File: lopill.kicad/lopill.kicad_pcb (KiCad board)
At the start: 2 copper layers, 23 x 59.5 mm, 34 parts, among them J1 Pins Left, J2 SWD, J3 USB_B_Micro, J4 Pins Right, SW1 Reset, U1 XC6206PxxxMR, U2 STM32L052C8Tx, Y1 8MHz, Y2 32.768KHz

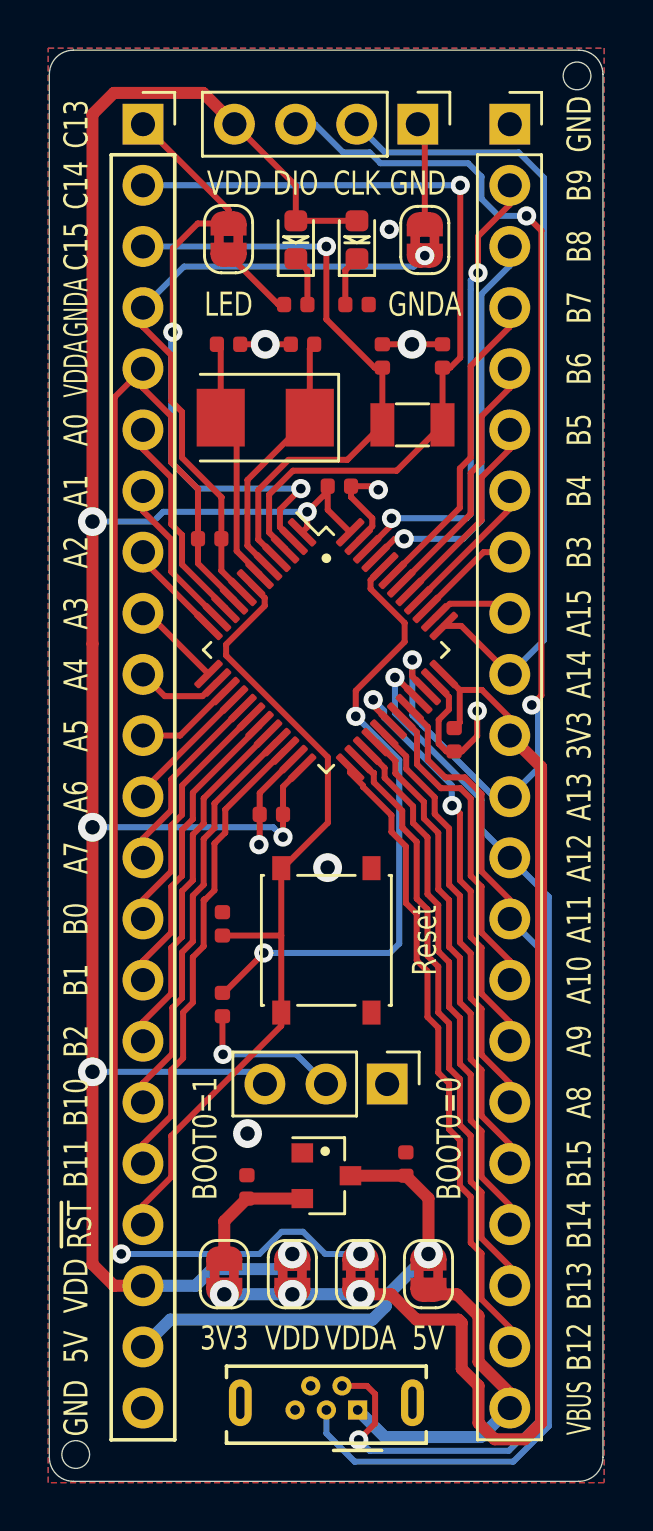
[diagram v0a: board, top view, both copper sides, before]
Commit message: Upgrade to KiCAD v6
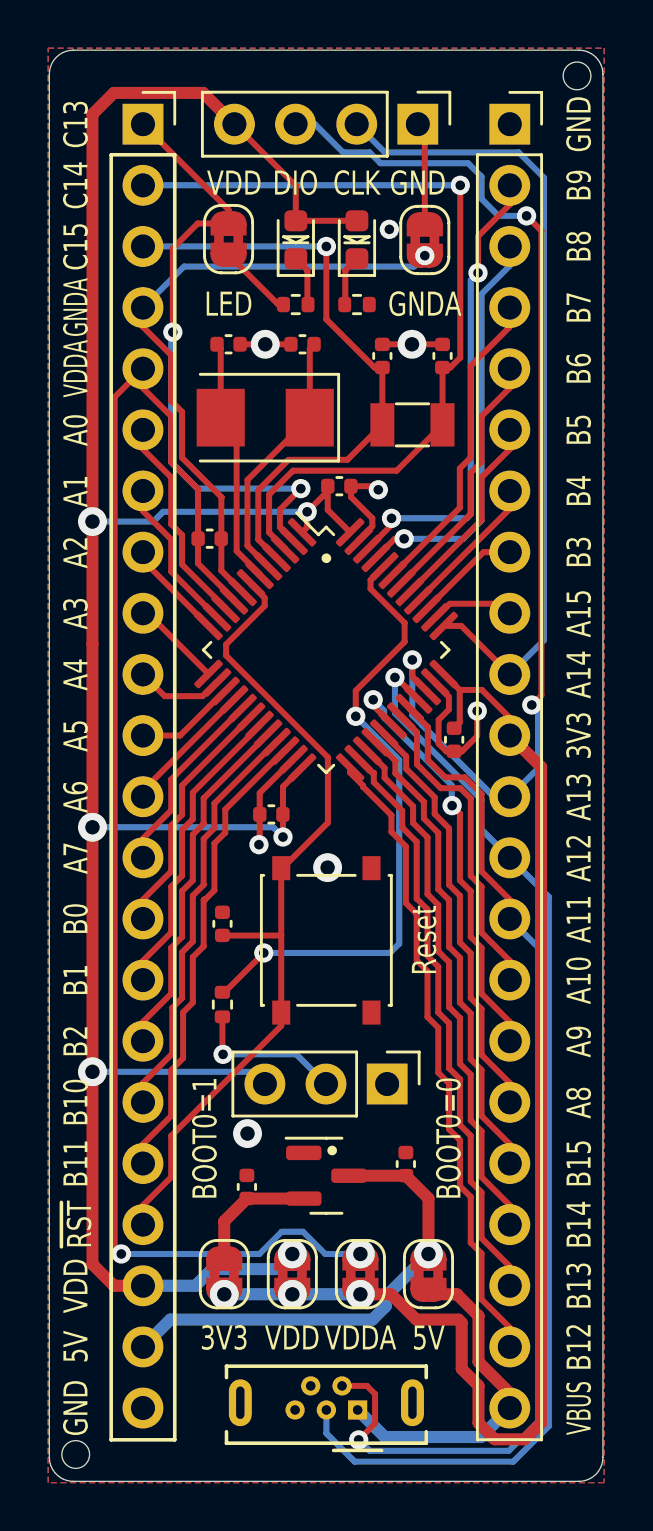
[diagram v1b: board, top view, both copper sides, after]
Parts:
- J3: footprint lopill:USB_Micro-B_HRO_U-D-M5DD-W-1_Vertical -> spbnick:USB_Micro-B_HRO_U-D-M5DD-W-1_Vertical
- REF** (x2): footprint lopill:Tooling_Hole -> spbnick:Tooling_Hole
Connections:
- J3 pad 4: Net-(J3-Pad4) -> unconnected-(J3-Pad4)
- J3 pad 6: GND -> unconnected-(J3-Pad6)
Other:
- net class Default removed
- net class Power removed

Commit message: Move footprints to the shared library
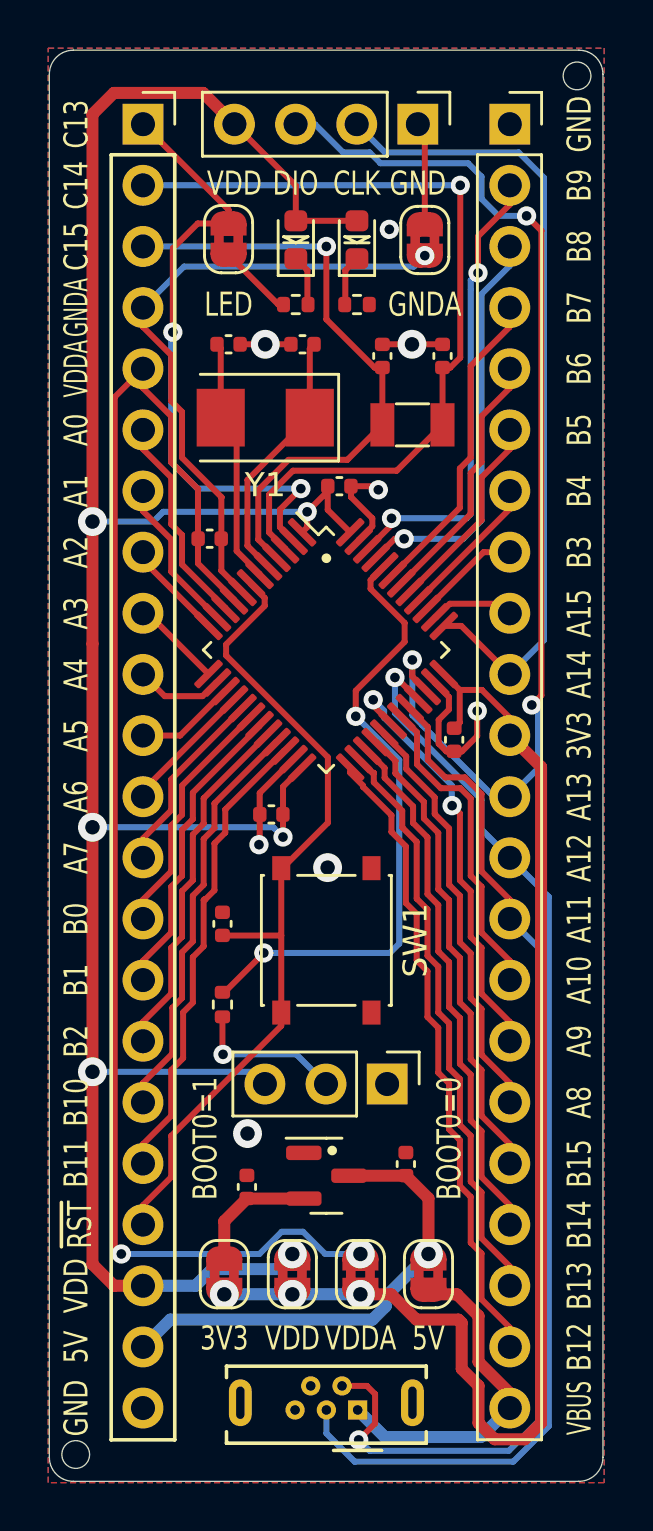
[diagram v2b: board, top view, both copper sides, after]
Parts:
- SW1: footprint lopill:SW_Push_1P1T_NO_5.1x5.1mm_H2.5mm -> spbnick:SW_Push_1P1T_NO_5.1x5.1mm_H2.5mm
- Y1: footprint lopill:Crystal_SMD_5032-2Pin_5.0x3.2mm_YXC -> spbnick:Crystal_SMD_5032-2Pin_5.0x3.2mm_YXC
